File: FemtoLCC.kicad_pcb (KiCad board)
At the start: 4 copper layers, 76.2 x 95.2 mm, 110 parts, among them J1 UART Header, J10 Conn_01x02, J2 RJHSE508002, J3 SM04B-SRSS-TB, J4 PMOD, J5 Conn_01x02, J6 Conn_01x02, J7 Conn_01x02, J8 Conn_01x02, J9 Conn_01x03, P1 USB_C_Plug_USB2.0, Q1 AO3401A, SW1 SW_Push, U1 NCP1117-3.3_SOT223, U10 SN74HC253DR, U11 DRV8874PWPR, U12 HCPL-0630, U14 ESP32-C6-WROOM-1, U15 NCP1117-5.0_SOT223, U2 MCP2562-E-SN, U3 MCP23018x-x-SO, U4 SN74HC253DR, U5 DRV8874PWPR, U6 SN74HC253DR, U7 DRV8874PWPR, U8 SN74HC253DR, U9 DRV8874PWPR

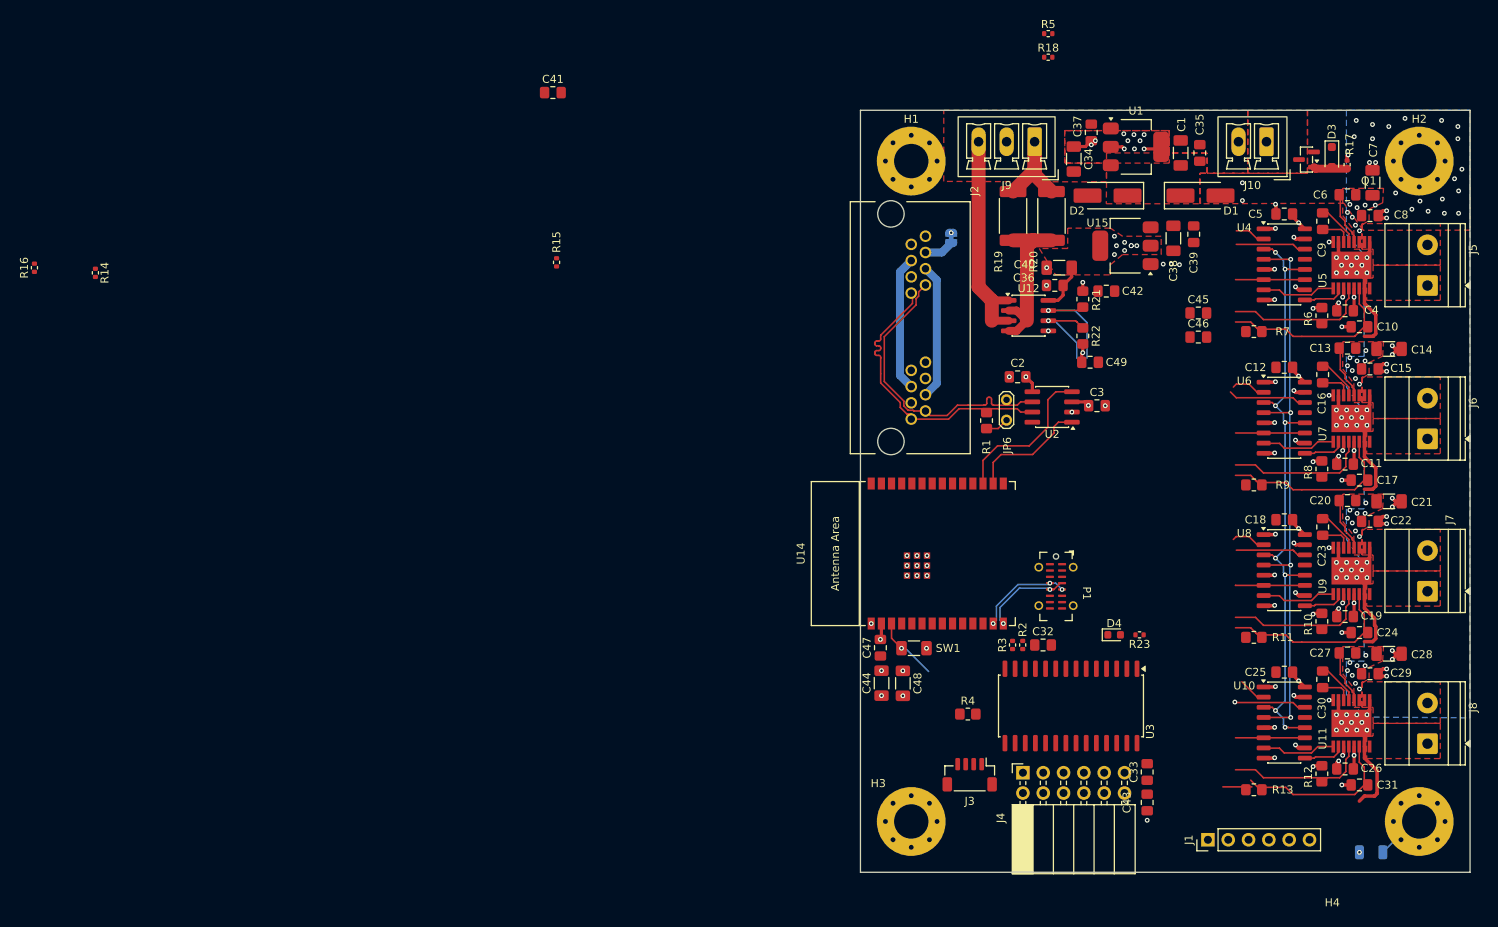
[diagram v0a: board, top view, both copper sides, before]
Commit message: Add fab pipeline, firmware, docs site, and tooling
- Makefile: kicad-cli gerber/drill/BOM/CPL/render exports, ERC/DRC, Hugo
  docs build, and firmware delegation to software/Makefile
- software/: ESP32-C6 Arduino firmware (channels, DCC source, expander,
  LCC traction, occupancy, throttle)
- site/: Hugo documentation site with GitHub Pages workflow
- tools/: BOM/CPL to JLCPCB converters, LCSC part map, stock checker
- production/: gerber bundle, board renders, ordering README
- .gitignore: firmware build output, __pycache__, upload staging,
  Hugo output, ERC/DRC reports; un-ignore tools/lcsc-parts.csv
- KiCad board, schematic, and DRV8874 footprint updates

Co-Authored-By: Claude Fable 5.1 <noreply@anthropic.com>
Claude-Session: https://claude.ai/code/session_01YbF1hVKFHpjgKwz3CaXtPo
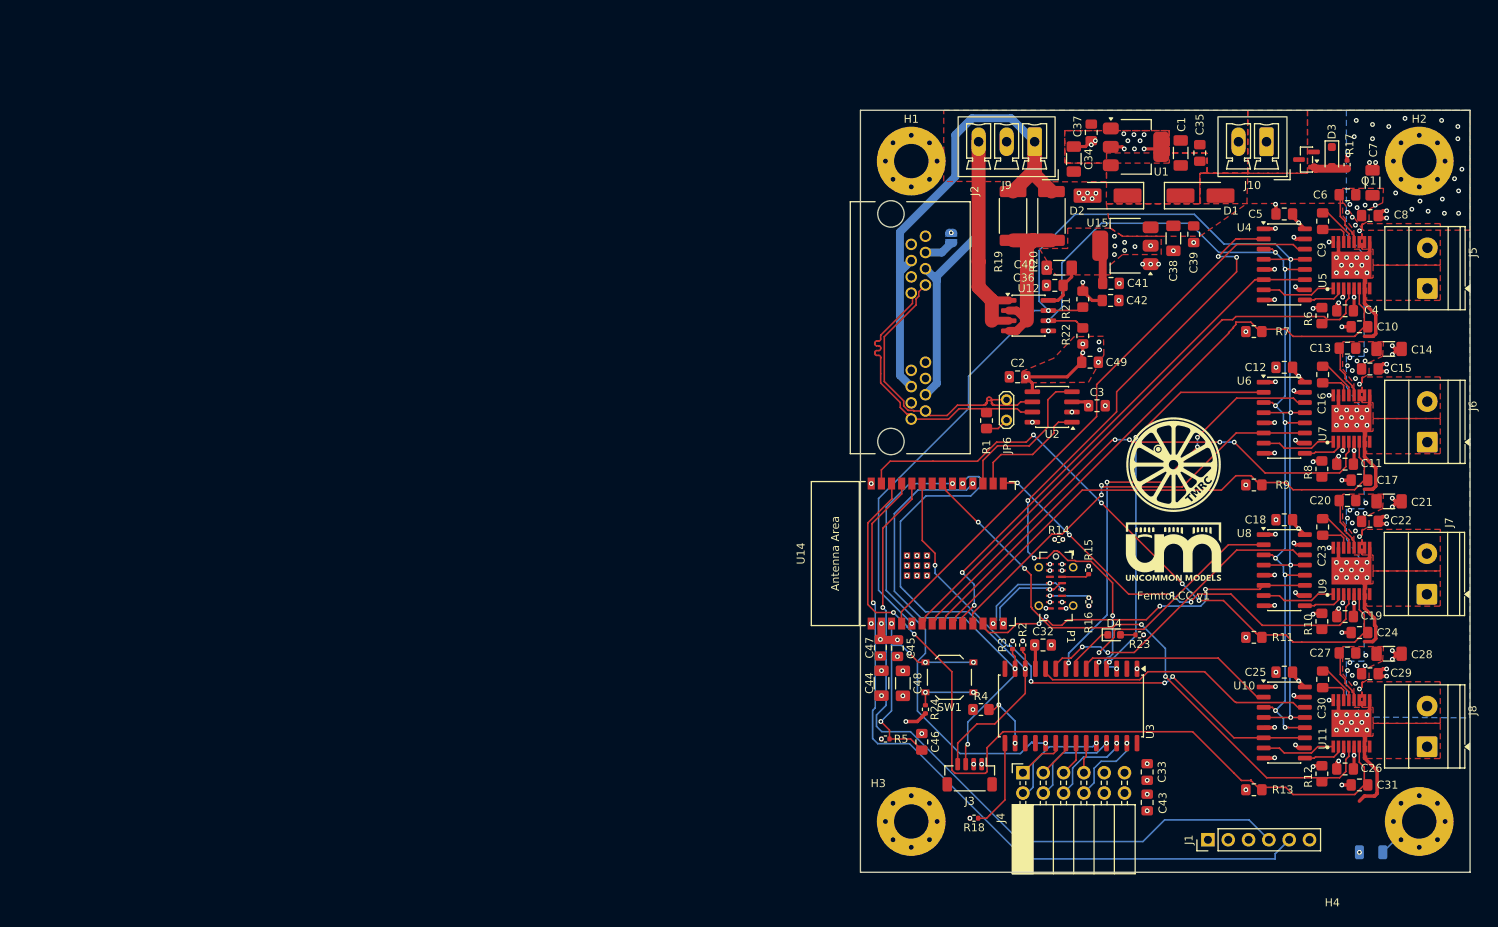
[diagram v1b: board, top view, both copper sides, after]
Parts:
- added R24: R2.2k, Resistor_SMD:R_0402_1005Metric, F.Cu at (159.0, 146.0)
- SW1: footprint Capacitor_SMD:C_1206_3216Metric_Pad1.33x1.80mm_HandSolder -> Button_Switch_SMD:SW_Push_1P1T_XKB_TS-1187A
- moved R16 138.3 mm to (179.4, 132.6)
- moved R14 124.9 mm to (175.7, 124.8), turned to 0 degrees
- moved R18 95.6 mm to (165.1, 159.6), turned to 180 degrees
- moved R5 90.5 mm to (154.0, 149.7)
- moved R15 76.8 mm to (179.4, 128.6)
- moved C41 73.7 mm to (182.2, 92.8)
- moved C46 61.3 mm to (158.5, 150.1), turned to -90 degrees
- moved C45 56.3 mm to (155.5, 138.4), turned to -90 degrees
- moved SW1 5.73 mm to (162.0, 142.0)
- moved R4 1.73 mm to (165.9, 146.0)
- moved C42 1.28 mm to (182.1, 94.9)
- moved J6 0.42 mm to (221.7, 112.6)
- moved J8 0.38 mm to (221.7, 150.7)
- moved J7 0.38 mm to (221.7, 131.6)
- moved J5 0.37 mm to (221.7, 93.4)
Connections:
- SW1 pad 1: GND -> Net-(R24-Pad1)
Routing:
- net /uart_tx: track 0.00 -> 93.4 mm, vias 0 -> 1
- net /dcc_p: track 85.5 -> 177.0 mm, vias 5 -> 6
- net /uart_rx: track 0.00 -> 89.7 mm, vias 0 -> 1
- net /sense_D: track 20.5 -> 107.3 mm, vias 0 -> 2
- net /dcc_en_A: track 3.85 -> 82.2 mm, vias 0 -> 6
- net /dir_A: track 8.82 -> 72.7 mm
- net /i2c_scl: track 0.00 -> 62.9 mm, vias 0 -> 2
- net /pwm_D: track 8.67 -> 68.4 mm, vias 0 -> 4
- net /sense_C: track 22.4 -> 80.2 mm, vias 0 -> 4
- net /i2c_sda: track 0.00 -> 57.2 mm, vias 0 -> 3
- net /pwm_A: track 8.67 -> 65.4 mm, vias 0 -> 2
- net /nFault_D: track 17.8 -> 74.2 mm, vias 0 -> 4
- net /I2Cint: track 0.00 -> 56.3 mm, vias 0 -> 2
- net /nFault_A: track 17.8 -> 72.9 mm
- net /sense_A: track 22.4 -> 75.3 mm
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- added copper zone on In2.Cu, net VBUS
- removed copper zone on In2.Cu, net /pwr_n
- removed copper zone on In2.Cu, net /pwr_p
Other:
- board text added: "FemtoLCC v1"
